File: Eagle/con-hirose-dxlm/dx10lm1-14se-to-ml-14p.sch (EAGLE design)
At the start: 2 parts, among them X1 HIROSE-DX10LM1-14SE

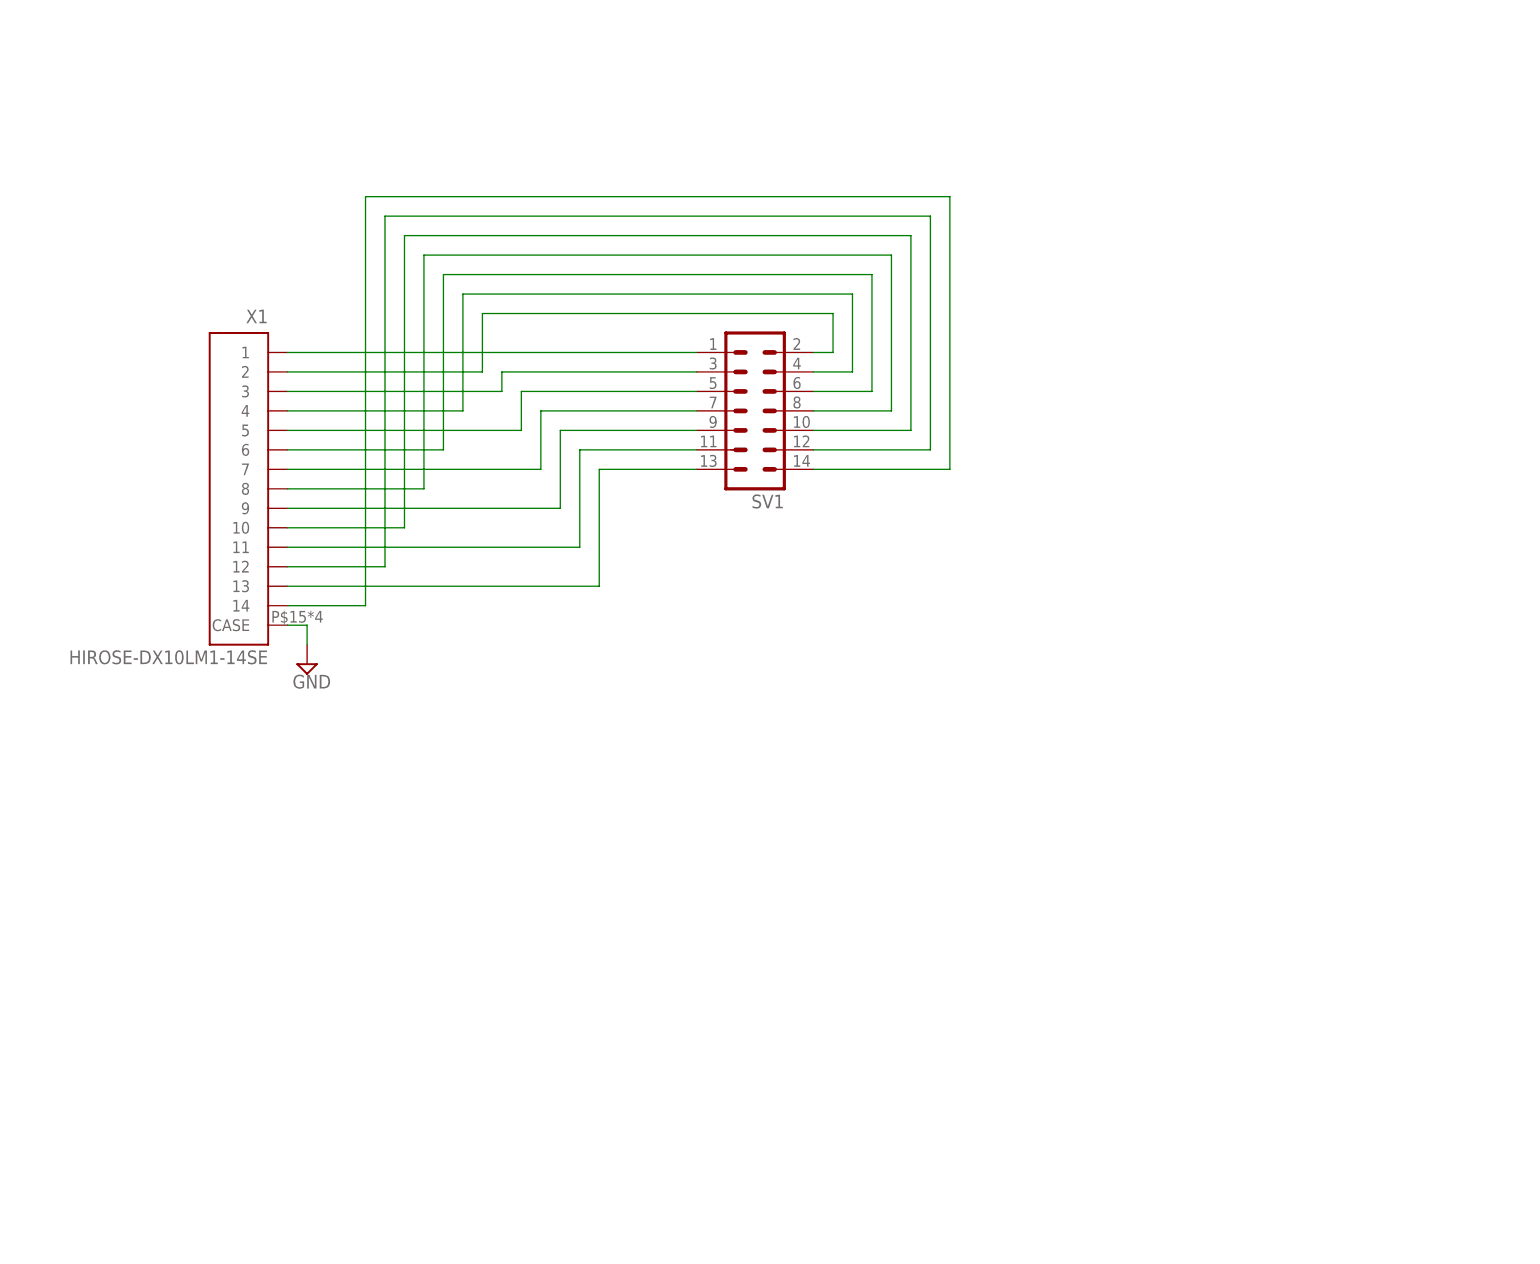
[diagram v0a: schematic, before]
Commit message: Renewed D2ML adaptor.
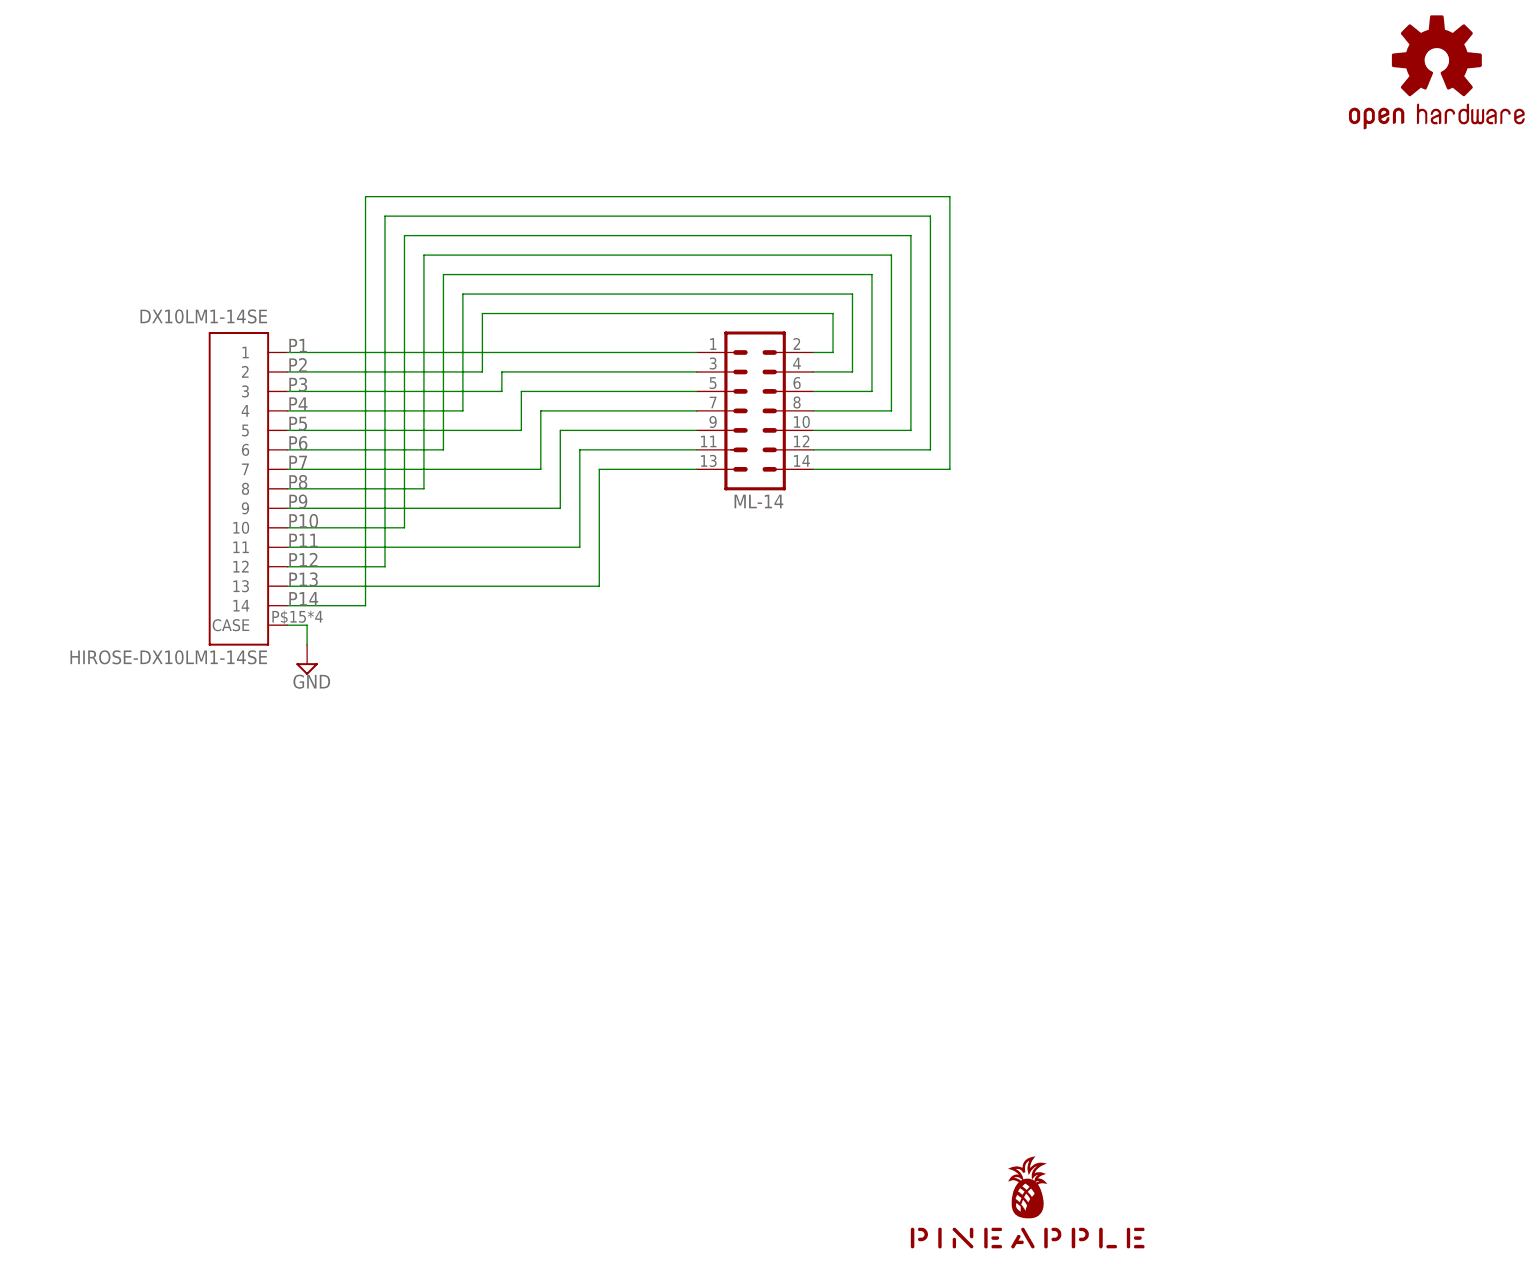
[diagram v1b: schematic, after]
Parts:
- added LOGO1: OSHW-LOGOS-COPPER, SparkFun-Aesthetics:OSHW-LOGOS-COPPER
- added U$1: PINEAPPLE450_SILK, pineapple:PINEAPPLE450_SILK
- renumbered SV1 to ML-14, X1 to DX10LM1-14SE
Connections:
- net N$1 renamed P1
- net N$10 renamed P6
- net N$11 renamed P8
- net N$12 renamed P10
- net N$13 renamed P12
- net N$14 renamed P14
- net N$2 renamed P3
- net N$3 renamed P5
- net N$4 renamed P7
- net N$5 renamed P9
- net N$6 renamed P11
- net N$7 renamed P13
- net N$8 renamed P2
- net N$9 renamed P4
